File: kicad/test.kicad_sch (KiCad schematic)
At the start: 1 part

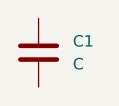
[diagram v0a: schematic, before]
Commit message: working single cap sch w/ an instance builder class
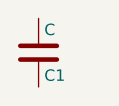
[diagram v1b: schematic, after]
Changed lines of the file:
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@@
   (symbol (lib_id "Device:C") (at 127 69.85 0) (unit 1)
     (in_bom yes) (on_board yes) (dnp no) (fields_autoplaced)
-    (property "Reference" "C1" (at 130.81 68.5799 0)
+    (property "Reference" "C1" (at 127.635 72.39 0)
       (effects (font (size 1.27 1.27)) (justify left))
     )
-    (property "Value" "C" (at 130.81 71.1199 0)
+    (property "Value" "C" (at 127.635 67.30999999999999 0)
       (effects (font (size 1.27 1.27)) (justify left))
     )
-    (property "Footprint" "" (at 127.9652 73.66 0)
-      (effects (font (size 1.27 1.27)) (justify left) hide)
+    (property "Footprint" "" (at 127.9652 66.03999999999999 0)
+      (effects (font (size 1.27 1.27)) hide)
     )
-    (property "Datasheet" "" (at 127 69.85 0)
-      (effects (font (size 1.27 1.27)) (justify left) hide)
+    (property "Datasheet" "~" (at 127 69.85 0)
+      (effects (font (size 1.27 1.27)) hide)
     )
     (property "Description" "Unpolarized capacitor" (at 127 69.85 0)
-      (effects (font (size 1.27 1.27)) (justify left) hide)
+      (effects (font (size 1.27 1.27)) hide)
     )
-    (pin "1")
-    (pin "2")
+    (property "ki_keywords" "cap capacitor" (at 127 69.85 0)
+      (effects (font (size 1.27 1.27)) hide)
+    )
+    (property "ki_fp_filters" "C_*" (at 127 69.85 0)
+      (effects (font (size 1.27 1.27)) hide)
+    )
     (instances
       (project ""
-        (path "/3ac9df30-75db-4ddb-8f86-237cc36e9594"
+        (path "/5443b932-203f-4864-8fab-a4b397151620"
           (reference "C1") (unit 1)
         )

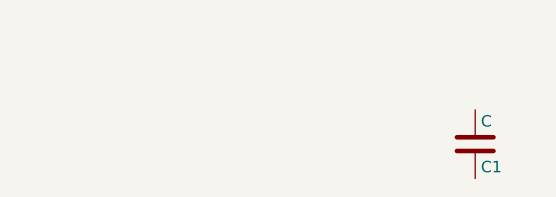
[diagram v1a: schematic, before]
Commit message: rough first pass at rotating props around symbol
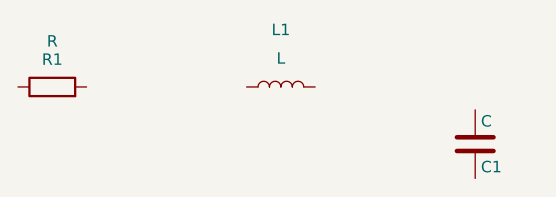
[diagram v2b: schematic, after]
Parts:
- added L1: L, symbol Device:L
- added R1: R, symbol Device:R
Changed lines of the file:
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@@
     (instances
       (project ""
-        (path "/5443b932-203f-4864-8fab-a4b397151620"
+        (path "/c6903e08-7bb7-4210-9bc3-e8fed23c7000"
           (reference "C1") (unit 1)
         )
       )
+    )
+  )
+  (symbol (lib_id "Device:L") (at 105.41 63.5 90) (unit 1)
+    (in_bom yes) (on_board yes) (dnp no) (fields_autoplaced)
+    (property "Reference" "L1" (at 105.41 57.15 90)
+      (effects (font (size 1.27 1.27)))
+    )
+    (property "Value" "L" (at 105.41 60.325 90)
+      (effects (font (size 1.27 1.27)))
+    )
+    (property "Footprint" "" (at 105.41 58.42 0)
+      (effects (font (size 1.27 1.27)) hide)
+    )
+    (property "Datasheet" "~" (at 105.41 58.42 0)
+      (effects (font (size 1.27 1.27)) hide)
+    )
+    (property "Description" "Inductor" (at 105.41 58.42 0)
+      (effects (font (size 1.27 1.27)) hide)
+    )
+    (property "ki_keywords" "inductor choke coil reactor magnetic" (at 105.41 58.42 0)
+      (effects (font (size 1.27 1.27)) hide)
+    )
+    (property "ki_fp_filters" "Choke_* *Coil* Inductor_* L_*" (at 105.41 58.42 0)
+      (effects (font (size 1.27 1.27)) hide)
+    )
+    (instances
+      (project ""
+        (path "/c6903e08-7bb7-4210-9bc3-e8fed23c7000"
+          (reference "L1") (unit 1)
+        )
+      )
+    )
+  )
+  (symbol (lib_id "Device:R") (at 80.01 63.5 90) (unit 1)
+    (in_bom yes) (on_board yes) (dnp no) (fields_autoplaced)
+    (property "Reference" "R1" (at 80.01 60.452 90)
+      (effects (font (size 1.27 1.27)))
+    )
+    (property "Value" "R" (at 80.01 58.42 90)
+      (effects (font (size 1.27 1.27)))
+    )
+    (property "Footprint" "" (at 80.01 56.642 90)
+      (effects (font (size 1.27 1.27)) hide)
+    )
+    (property "Datasheet" "~" (at 80.01 58.42 0)
+      (effects (font (size 1.27 1.27)) hide)
+    )
+    (property "Description" "Resistor" (at 80.01 58.42 0)
+      (effects (font (size 1.27 1.27)) hide)
+    )
+    (property "ki_keywords" "R res resistor" (at 80.01 58.42 0)
+      (effects (font (size 1.27 1.27)) hide)
+    )
+    (property "ki_fp_filters" "R_*" (at 80.01 58.42 0)
+      (effects (font (size 1.27 1.27)) hide)
+    )
+    (instances
+      (project ""
+        (path "/c6903e08-7bb7-4210-9bc3-e8fed23c7000"
+          (reference "R1") (unit 1)
+        )
+      )

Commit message: added direct wire draw between pins; added some temp position transforms and operators
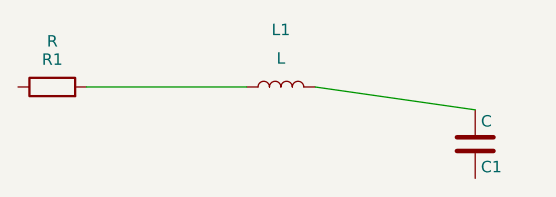
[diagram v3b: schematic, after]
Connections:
- net at C1.1: now also L1.2
- net at L1.1: now also R1.2
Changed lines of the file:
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@@
 (kicad_sch (version 20211014) (generator kiutils)
   (paper "A4")
+  (wire (pts (xy 83.82 63.5) (xy 101.6 63.5))
+    (stroke (width 0))
+  )
+  (wire (pts (xy 127 66.04) (xy 109.22 63.5))
+    (stroke (width 0))
+  )
   (symbol (lib_id "Device:C") (at 127 69.85 0) (unit 1)
     (in_bom yes) (on_board yes) (dnp no) (fields_autoplaced)
@@
       (effects (font (size 1.27 1.27)) hide)
     )
+    (pin "1")
+    (pin "2")
     (instances
       (project ""
-        (path "/c6903e08-7bb7-4210-9bc3-e8fed23c7000"
+        (path "/45e10f6c-35c7-40e6-8cd5-e849f87dcbda"
           (reference "C1") (unit 1)
         )
@@
       (effects (font (size 1.27 1.27)) hide)
     )
+    (pin "1")
+    (pin "2")
     (instances
       (project ""
-        (path "/c6903e08-7bb7-4210-9bc3-e8fed23c7000"
+        (path "/45e10f6c-35c7-40e6-8cd5-e849f87dcbda"
           (reference "L1") (unit 1)
         )
@@
       (effects (font (size 1.27 1.27)) hide)
     )
+    (pin "1")
+    (pin "2")
     (instances
       (project ""
-        (path "/c6903e08-7bb7-4210-9bc3-e8fed23c7000"
+        (path "/45e10f6c-35c7-40e6-8cd5-e849f87dcbda"
           (reference "R1") (unit 1)
         )
